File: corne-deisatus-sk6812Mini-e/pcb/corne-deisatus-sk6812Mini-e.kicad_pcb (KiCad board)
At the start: 2 copper layers, 149.4 x 94.7 mm, 98 parts, among them J1 MJ-4PP-9, J2 OLED, J3 LED, P1 i2c-pin, P2 i2c-pin, SW1 SW_PUSH, SW10 SW_PUSH, SW11 SW_PUSH, SW12 SW_PUSH, SW13 SW_PUSH, SW14 SW_PUSH, SW15 SW_PUSH, SW16 SW_PUSH, SW17 SW_PUSH, SW18 SW_PUSH, SW19 SW_PUSH, SW2 SW_PUSH, SW20 SW_PUSH, SW21 SW_PUSH, SW22 SW_PUSH, SW3 SW_PUSH, SW4 SW_PUSH, SW5 SW_PUSH, SW6 SW_PUSH, SW7 SW_PUSH, SW8 SW_PUSH, SW9 SW_PUSH, U1 ProMicro

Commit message: re adding tracks
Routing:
- net VCC: track 216.7 -> 744.5 mm, vias 17 -> 50
- net col0: track 97.7 -> 203.6 mm, vias 1 -> 4
- net col2: track 157.0 -> 242.2 mm, vias 3 -> 5
- net Net-(L4-Pad1): track 3.39 -> 48.6 mm, vias 1 -> 3
- net Net-(L12-Pad4): track 24.9 -> 68.7 mm, vias 2 -> 6
- net Net-(L24-Pad4): track 6.97 -> 49.0 mm, vias 2 -> 4
- net col3: track 195.5 -> 235.7 mm, vias 5 -> 9
- net Net-(L18-Pad4): track 6.41 -> 43.0 mm, vias 2 -> 5
- net Net-(L5-Pad1): track 3.52 -> 39.9 mm, vias 1 -> 4
- net Net-(L15-Pad4): track 6.46 -> 42.7 mm, vias 2 -> 4
- net Net-(L14-Pad4): track 3.23 -> 38.8 mm, vias 1 -> 4
- net Net-(L11-Pad4): track 6.49 -> 40.8 mm
- net Net-(L20-Pad4): track 6.50 -> 40.7 mm, vias 2 -> 4
- net Net-(L2-Pad3): track 6.77 -> 40.9 mm, vias 2 -> 4
- net Net-(L1-Pad3): track 6.77 -> 40.7 mm, vias 2 -> 3
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
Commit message: re adding tracks
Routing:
- net VCC: track 744.5 -> 839.8 mm, vias 50 -> 60
- net Net-(L22-Pad4): track 6.43 -> 64.2 mm, vias 2 -> 5
- net Net-(L7-Pad4): track 6.52 -> 47.7 mm, vias 2 -> 6
- net LED: track 74.4 -> 79.0 mm
- net row3: track 149.2 -> 150.4 mm, vias 3 -> 5

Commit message: tracks done
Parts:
- moved L27 0.98 mm to (178.3, 132.4)
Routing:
- net GND: track 77.0 -> 490.0 mm, vias 15 -> 103
- net Net-(L12-Pad4): track 68.7 -> 45.4 mm, vias 6 -> 5
- net VCC: track 839.8 -> 860.3 mm, vias 60 -> 64
- net col0: track 203.6 -> 221.1 mm, vias 4 -> 10
- net row3: track 150.4 -> 166.6 mm, vias 5 -> 6
- net col1: track 198.4 -> 214.1 mm, vias 4 -> 6
- net col3: track 235.7 -> 244.6 mm
- net col4: track 187.1 -> 195.0 mm
- net Net-(L10-Pad4): track 35.5 -> 42.0 mm, vias 3 -> 6
- net Net-(D8-Pad2): track 12.5 -> 17.2 mm
- net col2: track 242.2 -> 246.8 mm
- net row1: track 161.1 -> 165.7 mm, vias 3 -> 5
- net col5: track 195.4 -> 198.8 mm, vias 4 -> 5
- net Net-(D10-Pad2): track 15.9 -> 18.6 mm
- net Net-(L2-Pad3): track 40.9 -> 43.1 mm
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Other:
- outline, holes or cut-outs redrawn

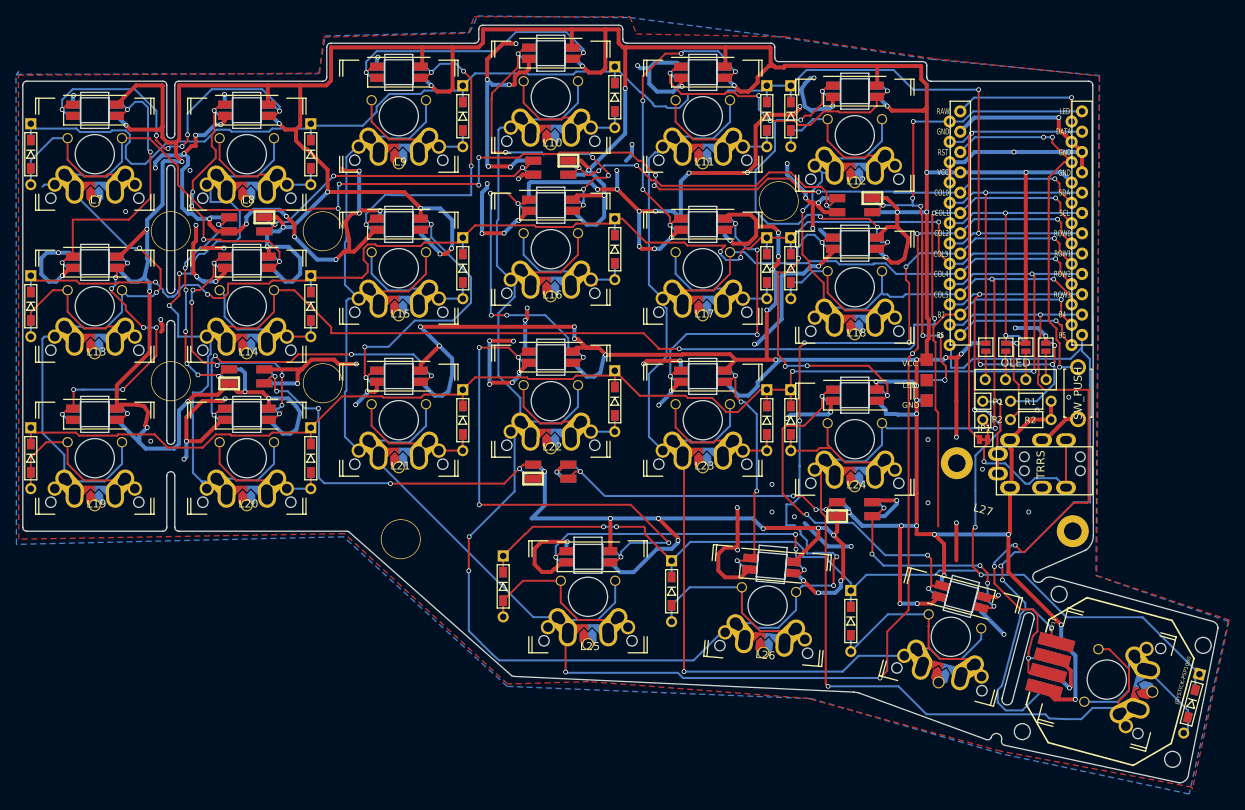
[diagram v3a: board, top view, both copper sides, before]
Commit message: removed unneeded cuts, updated gerber
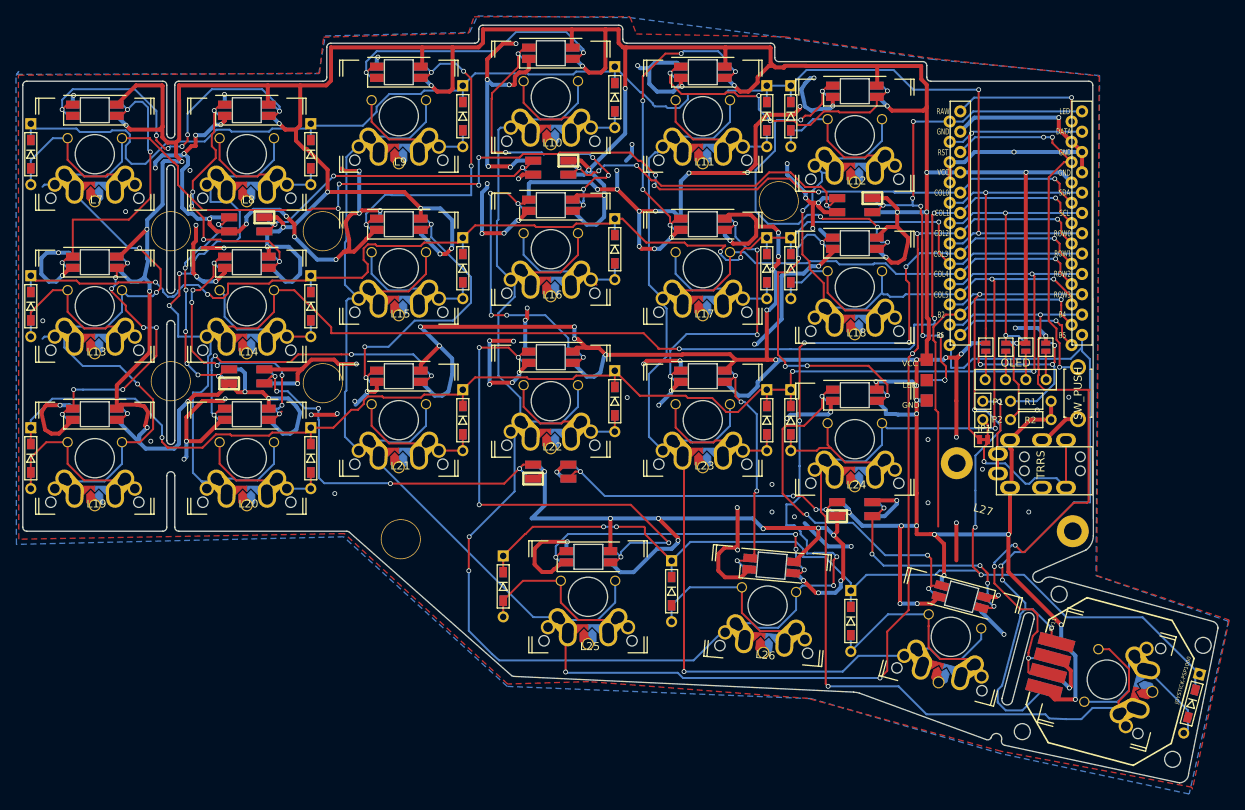
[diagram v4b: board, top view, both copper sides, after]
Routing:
- net GND: track 490.0 -> 503.0 mm, vias 103 -> 108
- net col0: track 221.1 -> 227.2 mm, vias 10 -> 11
- net row2: track 178.4 -> 184.2 mm, vias 3 -> 4
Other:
- outline, holes or cut-outs redrawn

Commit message: added footprint
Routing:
- net row2: track 184.2 -> 196.4 mm
- net row1: track 165.7 -> 177.9 mm
- net row0: track 181.9 -> 194.1 mm
- net row3: track 166.6 -> 174.9 mm
- net col4: track 195.0 -> 197.5 mm
- net Net-(D21-Pad2): track 23.0 -> 25.1 mm
- net Net-(D9-Pad2): track 17.7 -> 19.7 mm
- net Net-(D8-Pad2): track 17.2 -> 19.2 mm
- net Net-(D7-Pad2): track 21.6 -> 23.7 mm
- net Net-(D4-Pad2): track 17.7 -> 19.7 mm
- net Net-(D3-Pad2): track 17.2 -> 19.2 mm
- net Net-(D22-Pad2): track 22.4 -> 24.5 mm
- net Net-(D20-Pad2): track 26.4 -> 28.4 mm
- net Net-(D2-Pad2): track 17.7 -> 19.7 mm
- net Net-(D19-Pad2): track 24.0 -> 26.1 mm
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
